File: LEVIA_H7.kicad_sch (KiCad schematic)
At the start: 8 parts, among them U1 USBLC6-2P6

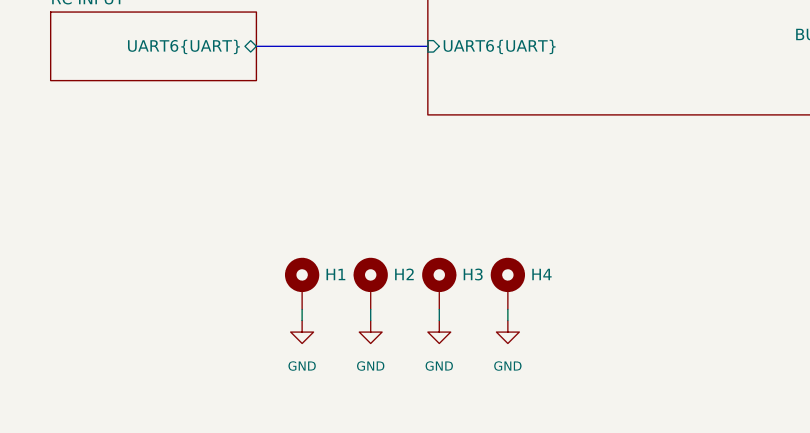
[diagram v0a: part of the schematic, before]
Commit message: BOM LCSC numbers assigned
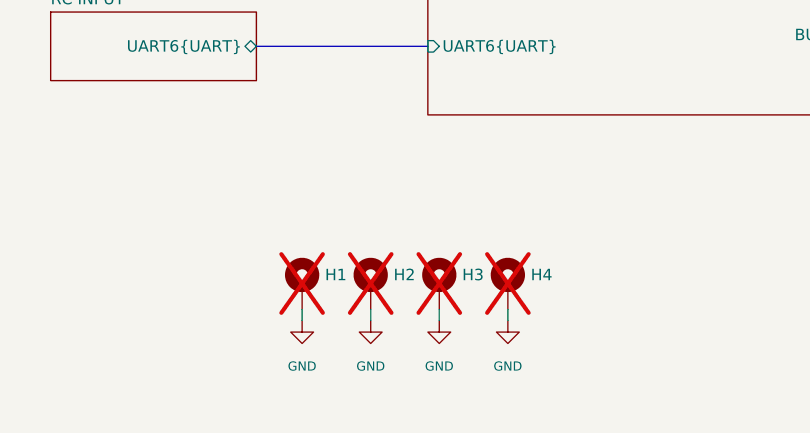
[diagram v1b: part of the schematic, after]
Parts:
- H1, H2, H3, H4: now not fitted
- R1, R2: LCSC Part (none) -> C25905
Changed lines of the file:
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@@
+			)
+		)
+		(property "LCSC Part" "C25905"
+			(at 72.39 45.72 90)
+			(hide yes)
+			(show_name no)
+			(do_not_autoplace no)
+			(effects
+				(font
+					(size 1.27 1.27)
+				)
 			)
 		)
@@
 			)
 		)
+		(property "LCSC Part" "C25905"
+			(at 72.39 48.26 90)
+			(hide yes)
+			(show_name no)
+			(do_not_autoplace no)
+			(effects
+				(font
+					(size 1.27 1.27)
+				)
+			)
+		)
 		(pin "2"
 		)
@@
 		(exclude_from_sim no)
 		(in_bom no)
-		(on_board yes)
+		(on_board no)
 		(in_pos_files no)
-		(dnp no)
+		(dnp yes)
 		(fields_autoplaced yes)
 		(property "Reference" "H2"
@@
 		(exclude_from_sim no)
 		(in_bom no)
-		(on_board yes)
+		(on_board no)
 		(in_pos_files no)
-		(dnp no)
+		(dnp yes)
 		(fields_autoplaced yes)
 		(property "Reference" "H1"
@@
 		(exclude_from_sim no)
 		(in_bom no)
-		(on_board yes)
+		(on_board no)
 		(in_pos_files no)
-		(dnp no)
+		(dnp yes)
 		(fields_autoplaced yes)
 		(property "Reference" "H3"
@@
 		(exclude_from_sim no)
 		(in_bom no)
-		(on_board yes)
+		(on_board no)
 		(in_pos_files no)
-		(dnp no)
+		(dnp yes)
 		(fields_autoplaced yes)
 		(property "Reference" "H4"
